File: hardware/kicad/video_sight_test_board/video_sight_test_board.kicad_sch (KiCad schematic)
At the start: 13 parts, among them Q1 AO3401A, SW1 SW_BATT, U1 XIAO-ESP32-S3, U2 TPS22919

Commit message: issue #1 #3 #4 対応
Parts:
- R3: value R_QOD -> 1kΩ
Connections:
- net EN: no longer U1.7 (GPIO43_D6_TX)
- net +3V3 renamed PERIPH_3V3
- net IN renamed XIAO_3V3
- new net PERIPH_EN: U1.7 (GPIO43_D6_TX)
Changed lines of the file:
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@@
 		)
 	)
-	(label "IN"
+	(label "XIAO_3V3"
 		(at 168.91 53.34 180)
 		(effects
@@
 		)
 	)
-	(label "IN"
+	(label "XIAO_3V3"
 		(at 110.49 156.21 0)
 		(effects
@@
 		)
 	)
-	(label "EN"
+	(label "PERIPH_EN"
 		(at 110.49 137.16 0)
 		(effects
@@
 			)
 		)
-		(property "Value" "R_QOD"
+		(property "Value" "1kΩ"
 			(at 226.06 58.166 90)
 			(effects
@@
 			)
 		)
-		(property "Value" "+3V3"
+		(property "Value" "PERIPH_3V3"
 			(at 250.19 41.91 0)
 			(effects

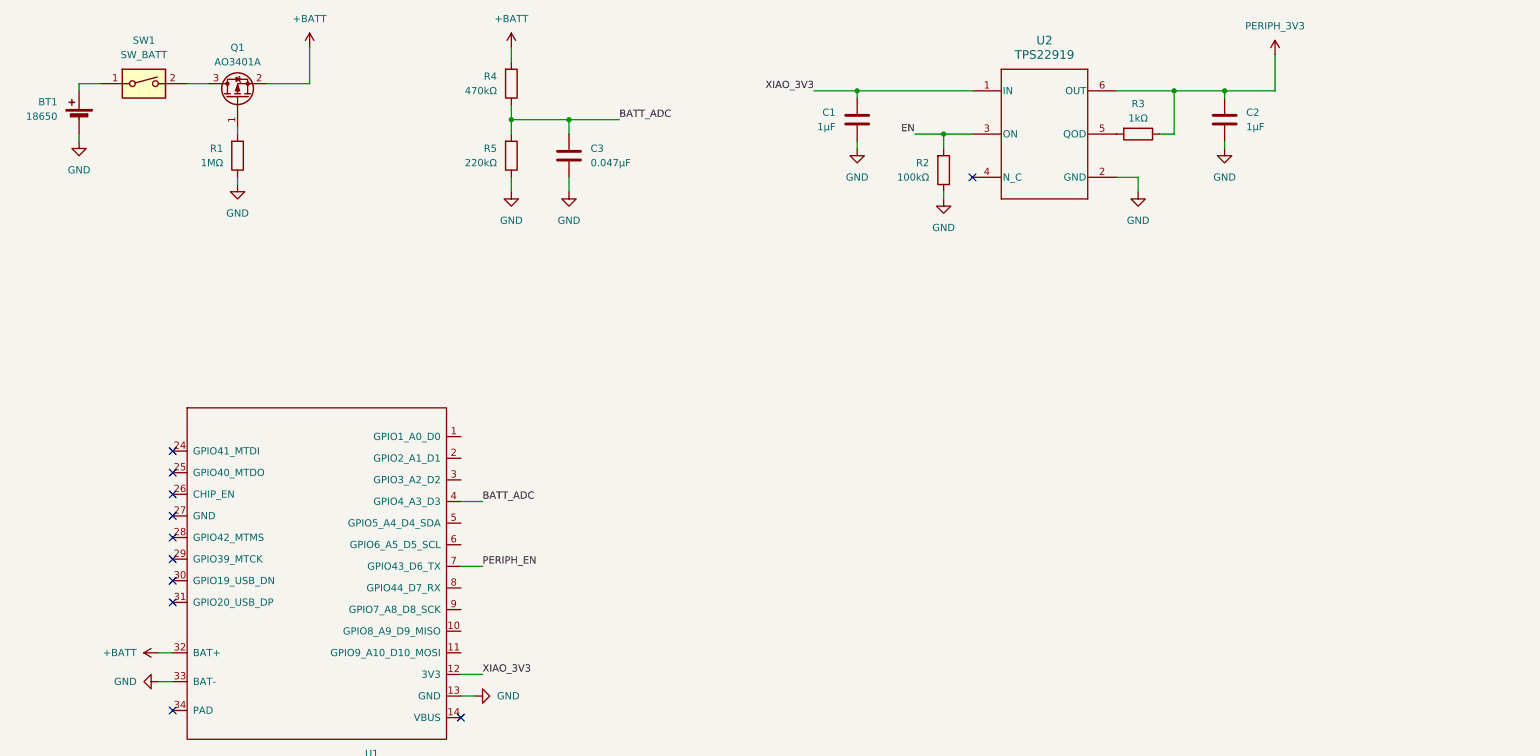
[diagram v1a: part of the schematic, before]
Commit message: XIAO ネットラベル追加 電流測定ジャンパー追加 PERIPH/XIAOバルクコンデンサ追加
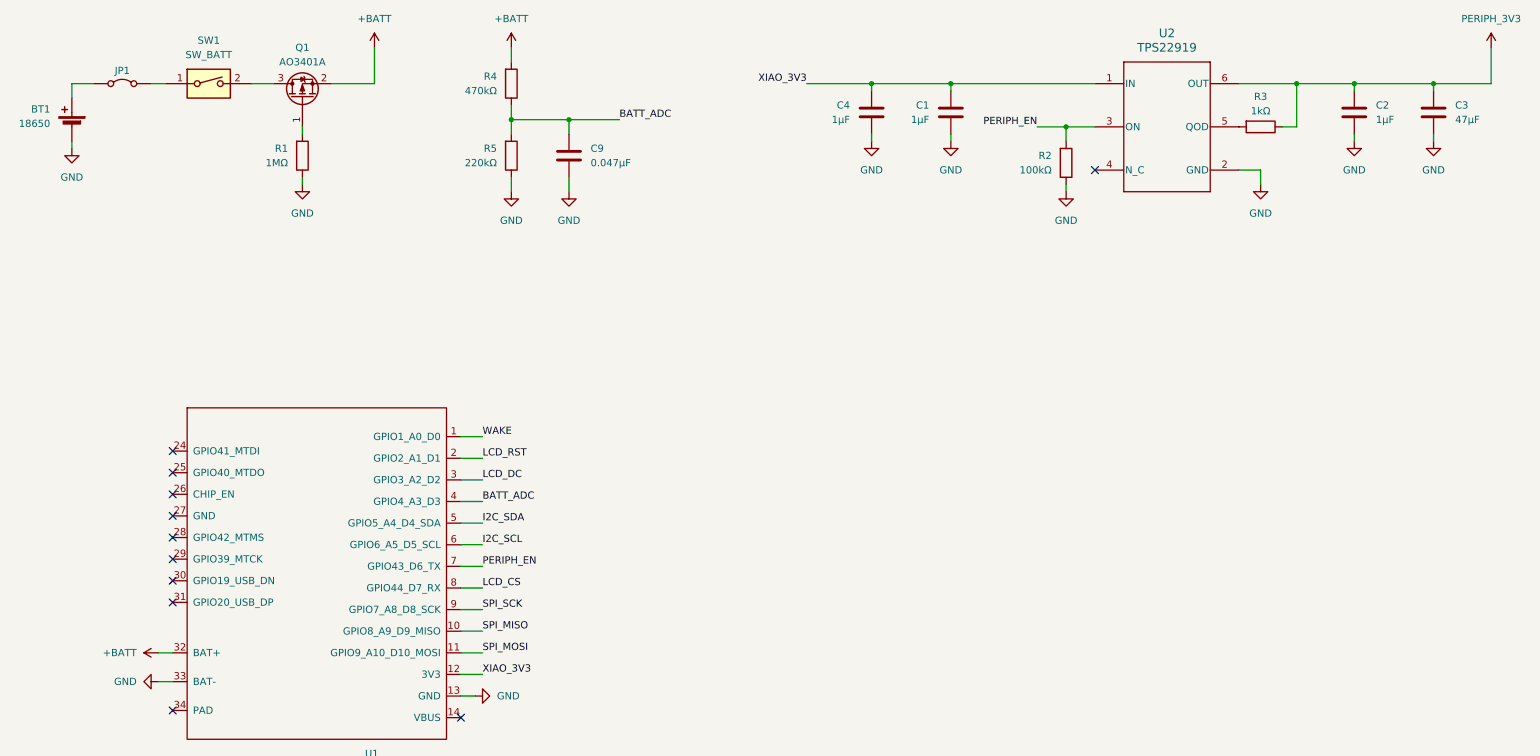
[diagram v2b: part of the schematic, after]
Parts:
- added C3: 47μF, symbol Device:C
- added C4: 1μF, symbol Device:C
- added JP1: CURRENT_TEST, TestPoint:TestPoint_2Pads_Pitch2.54mm_Drill0.8mm, symbol Jumper:Jumper_2_Bridged
- renumbered C3 to C9
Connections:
- net EN is gone; now on net PERIPH_EN: R2.2, U2.3 (ON)
- net GND: now also C3.2, C4.2
- net PERIPH_3V3: now also C3.1
- net XIAO_3V3: now also C4.1
- net at SW1.1: now also JP1.2 (B); no longer BT1.1 (+)
- net WAKE: now reaches U1.1 (GPIO1_A0_D0)
- net SPI_MISO: now reaches U1.10 (GPIO8_A9_D9_MISO)
- net SPI_MOSI: now reaches U1.11 (GPIO9_A10_D10_MOSI)
- net LCD_RST: now reaches U1.2 (GPIO2_A1_D1)
- net LCD_DC: now reaches U1.3 (GPIO3_A2_D2)
- net I2C_SDA: now reaches U1.5 (GPIO5_A4_D4_SDA)
- net I2C_SCL: now reaches U1.6 (GPIO6_A5_D5_SCL)
- net LCD_CS: now reaches U1.8 (GPIO44_D7_RX)
- net SPI_SCK: now reaches U1.9 (GPIO7_A8_D8_SCK)
- new net: BT1.1 (+), JP1.1 (A)
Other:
- moved on the sheet: BT1, C1, C2, Q1, R1, R2, R3, SW1, U2

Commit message: 回路図更新
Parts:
- added C5, C6, C7, C8: 0.1μF, symbol Device:C_Small
- added J1: BATTERY, symbol Connector:Conn_01x02_Pin
- added J2: XIAO_BREAKOUT_BOARD, symbol Connector_Generic:Conn_02x10_Odd_Even
- added J3: LCD, symbol Connector:Conn_01x08_Pin
- added J4: BNO055_MODULE, symbol Connector_Generic:Conn_02x04_Counter_Clockwise
- added J4: ATtiny1616_LEFT, symbol Connector:Conn_01x08_Pin
- added J5: ATtiny1616_RIGHT, symbol Connector:Conn_01x08_Pin
- added J6: INPUT_DEVICE, symbol Connector:Conn_01x06_Pin
- added SW2, SW3, SW4, SW5: SW_MEC_5G, symbol Switch:SW_MEC_5G
- added SW6: RotaryEncoder, symbol Device:RotaryEncoder
- added TP1: BAT+, symbol Connector:TestPoint
- added TP10: SPI_MOSI, symbol Connector:TestPoint
- added TP11: PERIPH_3V3, symbol Connector:TestPoint
- added TP12, TP2, TP7: GND, symbol Connector:TestPoint
- added TP3: BAT_SW, symbol Connector:TestPoint
- added TP4: XIAO_BAT, symbol Connector:TestPoint
- added TP5: XIAO_3V3, symbol Connector:TestPoint
- added TP6: PERIPH_EN, symbol Connector:TestPoint
- added TP8: GPIO42, symbol Connector:TestPoint
- added TP9: VBUS, symbol Connector:TestPoint
- added U3: ATtiny1616-S, Package_SO:SOIC-20W_7.5x12.8mm_P1.27mm, symbol MCU_Microchip_ATtiny:ATtiny1616-S
- BT1, U1: now not fitted
- C1, C2, C3, C4, C9: symbol Device:C -> Device:C_Small
- JP1: value CURRENT_TEST -> BATT_CURRENT
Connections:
- net +BATT: now also J2.20 (Pin_20), TP4.1
- net BATT_ADC: now also J2.17 (Pin_17)
- net GND: now also C5.1, C6.1, C7.1, C8.1, J1.2 (Pin_2), J2.19 (Pin_19), J2.2 (Pin_2), J3.2 (Pin_2), J4.2 (Pin_2), J4.7 (Pin_7), SW2.3 (B), SW2.4 (B), SW3.3 (B), SW3.4 (B), SW4.3 (B), SW4.4 (B), SW5.3 (B), SW5.4 (B), SW6.C, TP12.1, TP2.1, TP7.1, U3.20 (GND); no longer BT1.2 (-)
- net I2C_SCL: now also J2.9 (Pin_9), J4.4 (Pin_4), U3.11 (PB0)
- net I2C_SDA: now also J2.7 (Pin_7), J4.3 (Pin_3), U3.10 (PB1)
- net LCD_CS: now also J2.12 (Pin_12), J3.5 (Pin_5)
- net LCD_DC: now also J2.14 (Pin_14), J3.6 (Pin_6)
- net LCD_RST: now also J2.16 (Pin_16), J3.7 (Pin_7)
- net PERIPH_3V3: now also C6.2, C7.2, C8.2, J3.1 (Pin_1), J4.1 (Pin_1), TP11.1, U3.1 (VCC)
- net PERIPH_EN: now also J2.3 (Pin_3), TP6.1
- net SPI_MOSI: now also J2.6 (Pin_6), J2.8 (Pin_8), J3.3 (Pin_3), TP10.1
- net SPI_SCK: now also J2.10 (Pin_10), J3.4 (Pin_4)
- net WAKE: now also J2.11 (Pin_11)
- net XIAO_3V3: now also C5.2, J2.1 (Pin_1), TP5.1
- net at Q1.3 (D), SW1.2: now also TP3.1
- net at JP1.1 (A): now also J1.1 (Pin_1), TP1.1; no longer BT1.1 (+)
- new net: J6.4 (Pin_4), SW5.1 (A), SW5.2 (A)
- new net: J6.5 (Pin_5), SW6.A
- new net: J6.6 (Pin_6), SW6.B
- new net: J6.1 (Pin_1), SW2.1 (A), SW2.2 (A)
- new net: J6.2 (Pin_2), SW3.1 (A), SW3.2 (A)
- new net: J6.3 (Pin_3), SW4.1 (A), SW4.2 (A)
- new net CAM_SCL: J2.15 (Pin_15)
- new net CAM_SDA: J2.13 (Pin_13)
- new net GPIO42: J2.5 (Pin_5), TP8.1
- new net IMU_2V8: J4.8 (Pin_8)
- new net IMU_INT: J4.6 (Pin_6)
- new net IMU_RESET: J4.5 (Pin_5)
- new net LCD_BL: J2.18 (Pin_18), J3.8 (Pin_8)
- new net PA0: J5.4 (Pin_4), U3.16 (~{RESET}/PA0)
- new net PA1: J5.3 (Pin_3), U3.17 (PA1)
- new net PA2: J5.2 (Pin_2), U3.18 (PA2)
- new net PA3: J5.1 (Pin_1), U3.19 (PA3)
- new net PA4: J4.1 (Pin_1), U3.2 (PA4)
- new net PA5: J4.2 (Pin_2), U3.3 (PA5)
- new net PA6: J4.3 (Pin_3), U3.4 (PA6)
- new net PA7: J4.4 (Pin_4), U3.5 (PA7)
- new net PB2: J4.8 (Pin_8), U3.9 (PB2)
- new net PB3: J4.7 (Pin_7), U3.8 (PB3)
- new net PB4: J4.6 (Pin_6), U3.7 (PB4)
- new net PB5: J4.5 (Pin_5), U3.6 (PB5)
- new net PC0: J5.8 (Pin_8), U3.12 (PC0)
- new net PC1: J5.7 (Pin_7), U3.13 (PC1)
- new net PC2: J5.6 (Pin_6), U3.14 (PC2)
- new net PC3: J5.5 (Pin_5), U3.15 (PC3)
- new net VBUS: J2.4 (Pin_4), TP9.1
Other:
- note added: "1.89INCH LCD DISPLAY"
- note added: "BATTERY"
- note added: "IMU MODULE"
- note added: "LOAD SWITCH"
- note added: "SUB MCU"
- note added: "XIAO ESP32S3 SENSE"
- moved on the sheet: C1, C2, C3, C4, C9, JP1, Q1, R1, R2, R3, R4, R5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

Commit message: テストボード回路図修正 SPI_MOSI 体裁
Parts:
- removed BT1: 18650, symbol Device:Battery_Cell
- removed U1: XIAO-ESP32-S3, Seeed_Studio_XIAO_Series:XIAO-ESP32-S3-SMD, symbol Seeed_Studio_XIAO_Series:XIAO-ESP32-S3-SMD
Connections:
- net SPI_MISO: now also J2.8 (Pin_8)
- net SPI_MOSI: no longer J2.8 (Pin_8)
- no-connect marks 11 -> 1
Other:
- moved on the sheet: TP6

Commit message: IMU未使用ピン TP追加 他
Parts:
- added TP13: IMU_2V8, symbol Connector:TestPoint
- added TP14: GND, symbol Connector:TestPoint
- added TP15: IMU_INT, symbol Connector:TestPoint
- added TP16: IMU_RESET, symbol Connector:TestPoint
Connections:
- net GND: now also TP14.1
- net IMU_2V8: now also TP13.1
- net IMU_INT: now also TP15.1
- net IMU_RESET: now also TP16.1
- net CAM_SCL: no longer names the net of J2.15 (Pin_15)
- net CAM_SDA: no longer names the net of J2.13 (Pin_13)
- no-connect marks 1 -> 3
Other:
- moved on the sheet: C6, J4

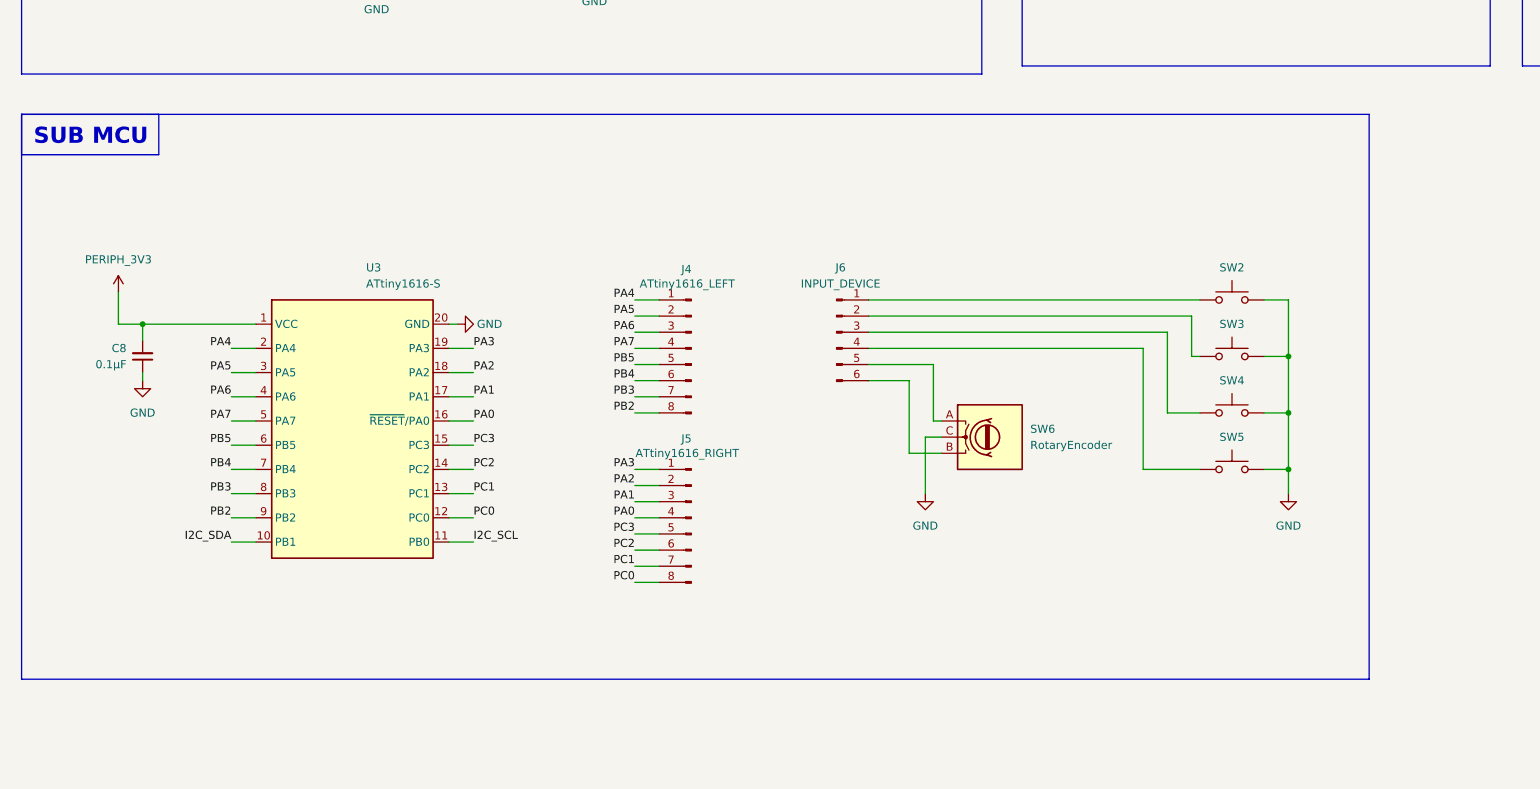
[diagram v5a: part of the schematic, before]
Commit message: UPDI書き込み端子追加 内部プルアップ注記追加
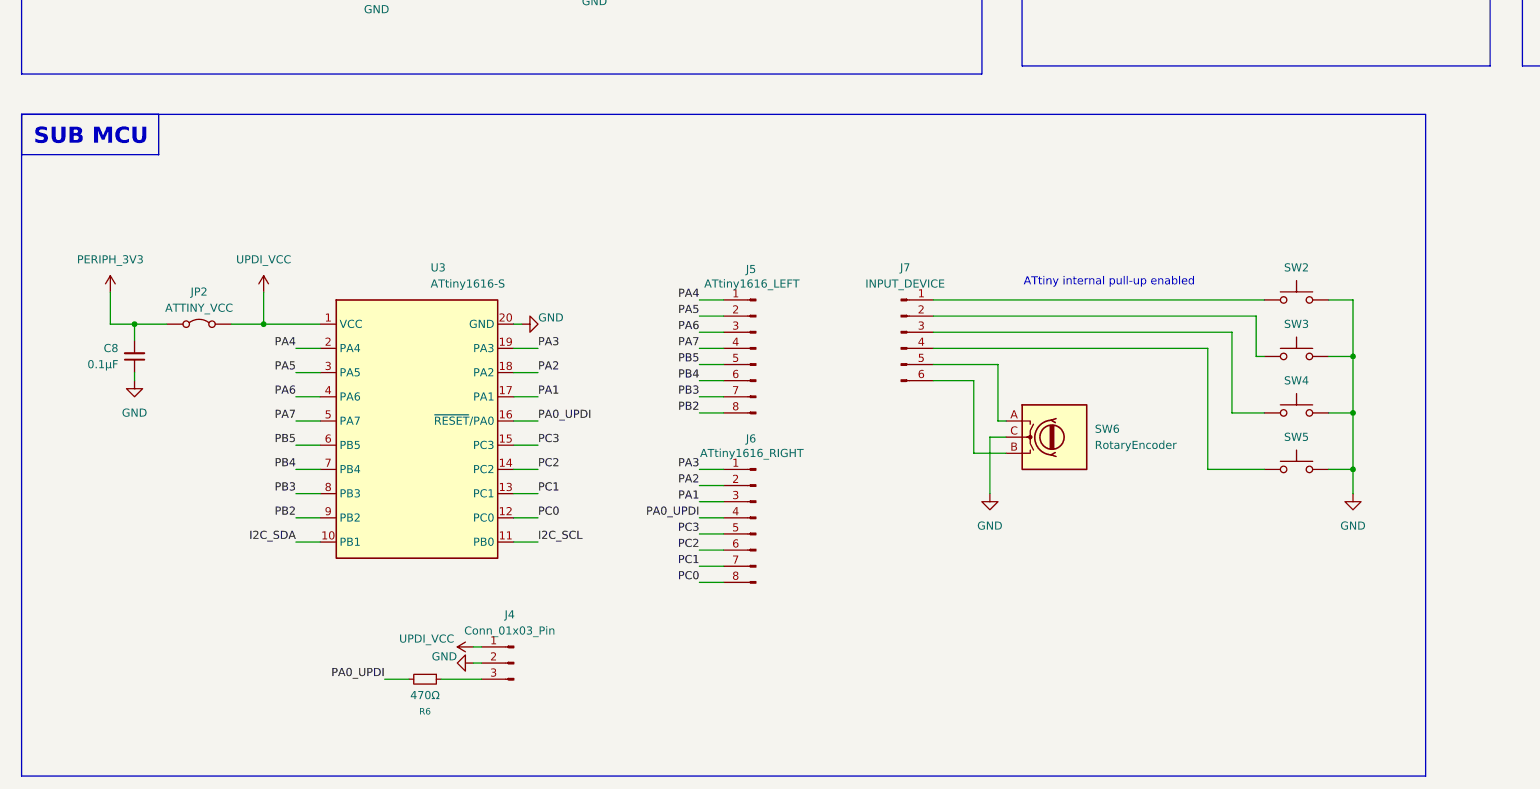
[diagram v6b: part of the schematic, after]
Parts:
- added J4: Conn_01x03_Pin, symbol Connector:Conn_01x03_Pin
- added JP2: ATTINY_VCC, TestPoint:TestPoint_2Pads_Pitch2.54mm_Drill0.8mm, symbol Jumper:Jumper_2_Bridged
- added R6: 470Ω, symbol Device:R_Small
- renumbered J4 to J5, J5 to J6, J6 to J7
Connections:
- net GND: now also J4.2 (Pin_2)
- net PERIPH_3V3: now also JP2.1 (A); no longer U3.1 (VCC)
- net PA0 renamed PA0_UPDI
- net PA0_UPDI: now also R6.2
- new net: J4.3 (Pin_3), R6.1
- new net UPDI_VCC: J4.1 (Pin_1), JP2.2 (B), U3.1 (VCC)
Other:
- note added: "ATtiny internal pull-up enabled"
- moved on the sheet: C8, J5, J6, J7, SW2, SW3, SW4, SW5, SW6, U3
